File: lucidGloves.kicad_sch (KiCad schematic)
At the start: 25 parts, among them J1 USB_C_Receptacle_PowerOnly_6P, J10 Conn_01x05_Male, J11 Conn_01x05_Male, J12 Conn_01x19_Female, J13 Conn_01x05_Male, J14 Conn_01x03_Male, J15 Conn_01x03_Male, J16 Conn_01x03_Male, J17 Conn_01x03_Male, J18 Conn_01x03_Male, J2 USB_C_Receptacle_PowerOnly_6P, J3 Conn_01x05_Male, J4 Conn_01x05_Male, J5 Conn_01x05_Male, J6 Conn_01x16_Male, J7 Conn_01x08_Male, J8 Conn_01x19_Female, J9 Conn_01x05_Male, SW1 SW_MEC_5E

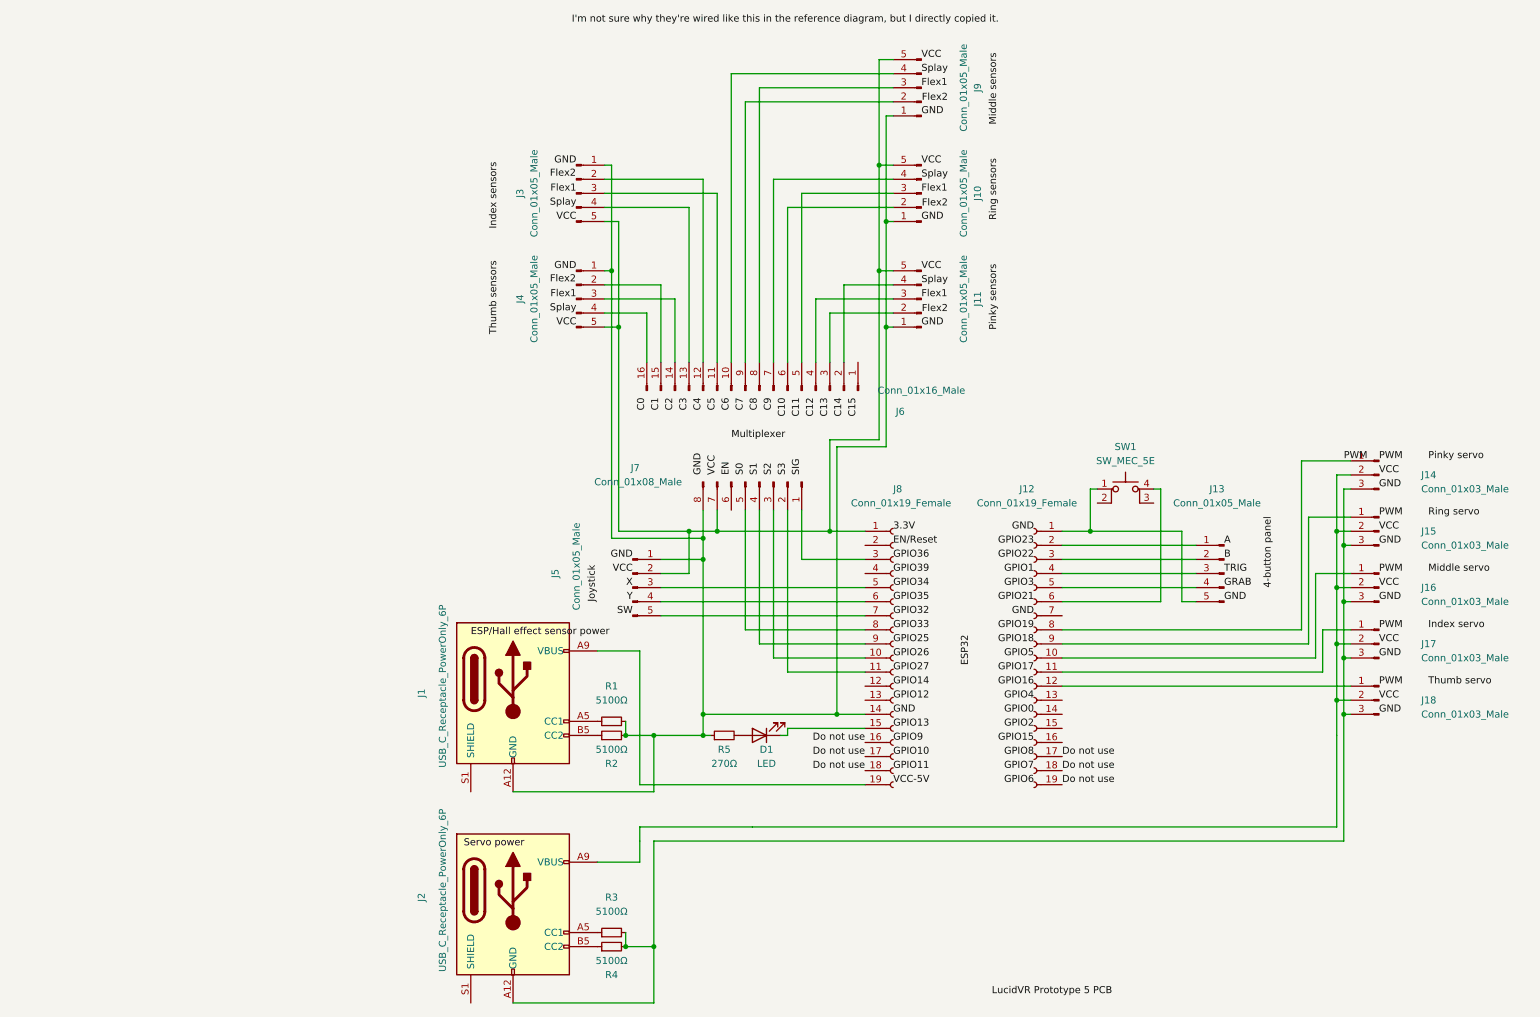
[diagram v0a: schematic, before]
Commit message: Fix all ERC errors and warnings
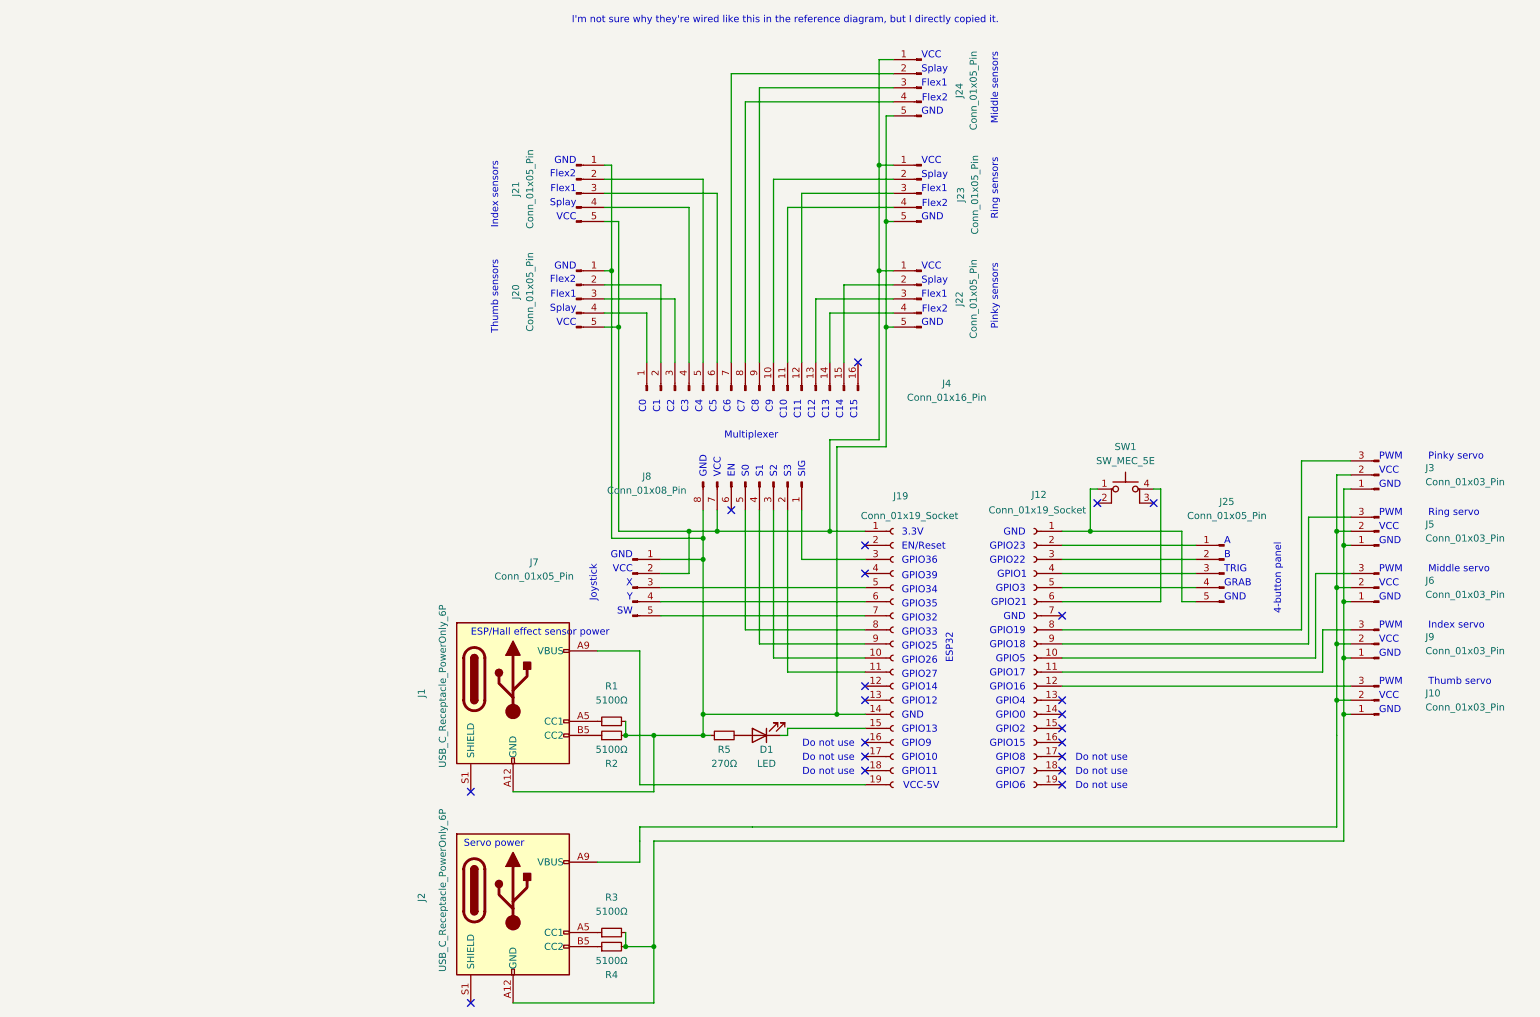
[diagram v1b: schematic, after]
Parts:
- removed J10, J11, J13, J3, J4, J5, J9: Conn_01x05_Male, symbol Connector:Conn_01x05_Male
- removed J12, J8: Conn_01x19_Female, symbol Connector:Conn_01x19_Female
- removed J14, J15, J16, J17, J18: Conn_01x03_Male, symbol Connector:Conn_01x03_Male
- removed J6: Conn_01x16_Male, symbol Connector:Conn_01x16_Male
- removed J7: Conn_01x08_Male, symbol Connector:Conn_01x08_Male
- added J10, J3, J5, J6, J9: Conn_01x03_Pin, symbol Connector:Conn_01x03_Pin
- added J12, J19: Conn_01x19_Socket, symbol Connector:Conn_01x19_Socket
- added J20, J21, J22, J23, J24, J25, J7: Conn_01x05_Pin, symbol Connector:Conn_01x05_Pin
- added J4: Conn_01x16_Pin, symbol Connector:Conn_01x16_Pin
- added J8: Conn_01x08_Pin, symbol Connector:Conn_01x08_Pin
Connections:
- net at J1.A12 (GND), J1.B12 (GND), R1.2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: now also J19.14 (Pin_14), J20.1 (Pin_1), J21.1 (Pin_1), J22.5 (Pin_5), J23.5 (Pin_5), J24.5 (Pin_5), J7.1 (Pin_1), J8.8 (Pin_8)
- net at D1.1 (K): now also J19.15 (Pin_15)
- net at J1.A9 (VBUS), J1.B9 (VBUS): now also J19.19 (Pin_19)
- net at J2.A9 (VBUS), J2.B9 (VBUS): now also J10.2 (Pin_2), J3.2 (Pin_2), J5.2 (Pin_2), J6.2 (Pin_2), J9.2 (Pin_2)
- net at J2.A12 (GND), J2.B12 (GND), R3.2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: now also J10.1 (Pin_1), J3.1 (Pin_1), J5.1 (Pin_1), J6.1 (Pin_1), J9.1 (Pin_1)
- net at SW1.1: now also J12.1 (Pin_1), J25.5 (Pin_5)
- net at SW1.4 (A): now also J12.6 (Pin_6)
- new net: J12.10 (Pin_10), J6.3 (Pin_3)
- new net: J12.11 (Pin_11), J9.3 (Pin_3)
- new net: J10.3 (Pin_3), J12.12 (Pin_12)
- new net: J12.2 (Pin_2), J25.1 (Pin_1)
- new net: J12.3 (Pin_3), J25.2 (Pin_2)
- new net: J12.4 (Pin_4), J25.3 (Pin_3)
- new net: J12.5 (Pin_5), J25.4 (Pin_4)
- new net: J12.8 (Pin_8), J3.3 (Pin_3)
- new net: J12.9 (Pin_9), J5.3 (Pin_3)
- new net: J19.1 (Pin_1), J20.5 (Pin_5), J21.5 (Pin_5), J22.1 (Pin_1), J23.1 (Pin_1), J24.1 (Pin_1), J7.2 (Pin_2), J8.7 (Pin_7)
- new net: J22.2 (Pin_2), J4.15 (Pin_15)
- new net: J22.3 (Pin_3), J4.13 (Pin_13)
- new net: J22.4 (Pin_4), J4.14 (Pin_14)
- new net: J20.2 (Pin_2), J4.2 (Pin_2)
- new net: J20.3 (Pin_3), J4.3 (Pin_3)
- new net: J20.4 (Pin_4), J4.1 (Pin_1)
- new net: J21.2 (Pin_2), J4.5 (Pin_5)
- new net: J21.3 (Pin_3), J4.6 (Pin_6)
- new net: J21.4 (Pin_4), J4.4 (Pin_4)
- new net: J19.5 (Pin_5), J7.3 (Pin_3)
- new net: J19.6 (Pin_6), J7.4 (Pin_4)
- new net: J19.7 (Pin_7), J7.5 (Pin_5)
- new net: J23.2 (Pin_2), J4.10 (Pin_10)
- new net: J23.3 (Pin_3), J4.12 (Pin_12)
- new net: J23.4 (Pin_4), J4.11 (Pin_11)
- new net: J19.3 (Pin_3), J8.1 (Pin_1)
- new net: J19.11 (Pin_11), J8.2 (Pin_2)
- new net: J19.10 (Pin_10), J8.3 (Pin_3)
- new net: J19.9 (Pin_9), J8.4 (Pin_4)
- new net: J19.8 (Pin_8), J8.5 (Pin_5)
- new net: J24.2 (Pin_2), J4.7 (Pin_7)
- new net: J24.4 (Pin_4), J4.8 (Pin_8)
- new net: J24.3 (Pin_3), J4.9 (Pin_9)
- no-connect marks 0 -> 21
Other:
- note added: "3.3V"
- note added: "4-button panel"
- note added: "A"
- note added: "B"
- note added: "C0"
- note added: "C1"
- note added: "C10"
- note added: "C11"
- note added: "C12"
- note added: "C13"
- note added: "C14"
- note added: "C15"
- note added: "C2"
- note added: "C3"
- note added: "C4"
- note added: "C5"
- note added: "C6"
- note added: "C7"
- note added: "C8"
- note added: "C9"
- note added: "Do not use"
- note added: "EN"
- note added: "EN/Reset"
- note added: "ESP/Hall effect sensor power"
- note added: "ESP32"
- note added: "Flex1"
- note added: "Flex2"
- note added: "GND"
- note added: "GPIO0"
- note added: "GPIO1"
- note added: "GPIO10"
- note added: "GPIO11"
- note added: "GPIO12"
- note added: "GPIO13"
- note added: "GPIO14"
- note added: "GPIO15"
- note added: "GPIO16"
- note added: "GPIO17"
- note added: "GPIO18"
- note added: "GPIO19"
- note added: "GPIO2"
- note added: "GPIO21"
- note added: "GPIO22"
- note added: "GPIO23"
- note added: "GPIO25"
- note added: "GPIO26"
- note added: "GPIO27"
- note added: "GPIO3"
- note added: "GPIO32"
- note added: "GPIO33"
- note added: "GPIO34"
- note added: "GPIO35"
- note added: "GPIO36"
- note added: "GPIO39"
- note added: "GPIO4"
- note added: "GPIO5"
- note added: "GPIO6"
- note added: "GPIO7"
- note added: "GPIO8"
- note added: "GPIO9"
- note added: "GRAB"
- note added: "I'm not sure why they're wired like this in the reference diagram, but I directly copied it."
- note added: "Index sensors"
- note added: "Index servo"
- note added: "Joystick"
- note added: "Middle sensors"
- note added: "Middle servo"
- note added: "Multiplexer"
- note added: "PWM"
- note added: "Pinky sensors"
- note added: "Pinky servo"
- note added: "Ring sensors"
- note added: "Ring servo"
- note added: "S0"
- note added: "S1"
- note added: "S2"
- note added: "S3"
- note added: "SIG"
- note added: "SW"
- note added: "Servo power"
- note added: "Splay"
- note added: "TRIG"
- note added: "Thumb sensors"
- note added: "Thumb servo"
- note added: "VCC"
- note added: "VCC-5V"
- note added: "X"
- note added: "Y"
- title: (none) -> LucidVR Prototype 5 PCB

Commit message: Add footprints to schematic
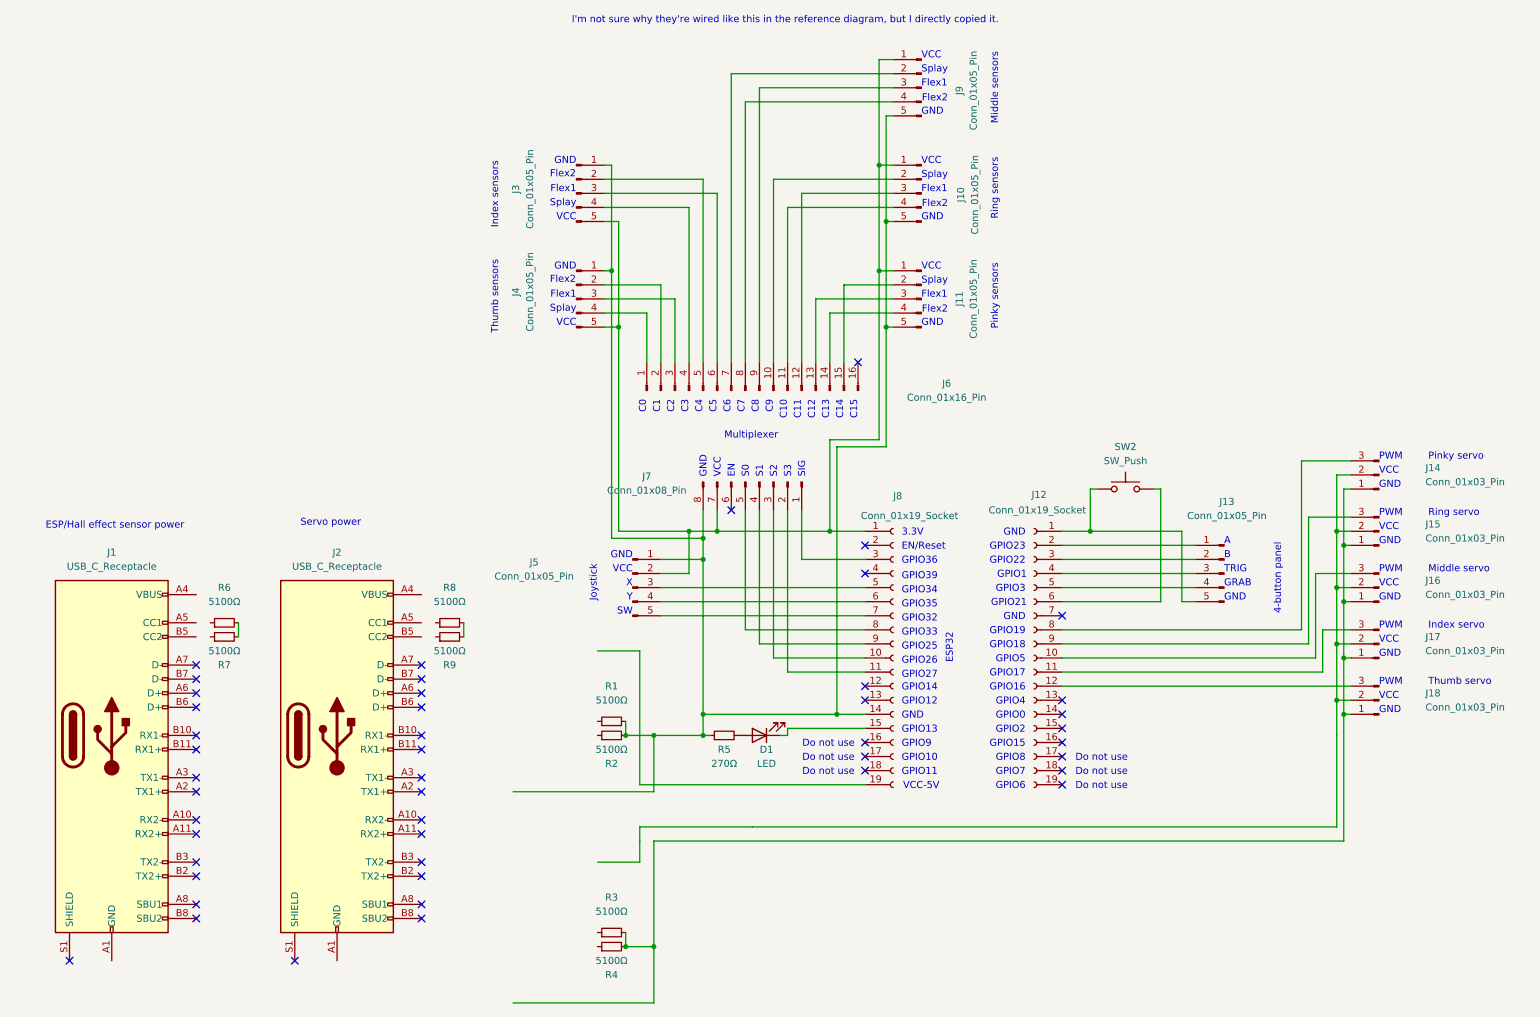
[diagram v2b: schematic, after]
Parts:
- removed J1, J2: USB_C_Receptacle_PowerOnly_6P, symbol Connector:USB_C_Receptacle_PowerOnly_6P
- removed SW1: SW_MEC_5E, symbol Switch:SW_MEC_5E
- added J1, J2: USB_C_Receptacle, symbol Connector:USB_C_Receptacle
- added R6, R7, R8, R9: 5100Ω, Resistor_SMD:R_0603_1608Metric, symbol Device:R_Small
- added SW2: SW_Push, Button_Switch_THT:SW_TH_Tactile_Omron_B3F-10xx, symbol Switch:SW_Push
- D1: footprint (none) -> LED_THT:LED_D5.0mm
- J10: renamed from J23; footprint (none) -> Connector_PinHeader_2.54mm:PinHeader_1x05_P2.54mm_Vertical
- J11: renamed from J22; footprint (none) -> Connector_PinHeader_2.54mm:PinHeader_1x05_P2.54mm_Vertical
- J12: footprint (none) -> Connector_PinSocket_2.54mm:PinSocket_1x19_P2.54mm_Vertical
- J13: renamed from J25; footprint (none) -> Connector_PinHeader_2.54mm:PinHeader_1x05_P2.54mm_Vertical
- J14: renamed from J3; footprint (none) -> Connector_PinHeader_2.54mm:PinHeader_1x03_P2.54mm_Vertical
- J15: renamed from J5; footprint (none) -> Connector_PinHeader_2.54mm:PinHeader_1x03_P2.54mm_Vertical
- J16: renamed from J6; footprint (none) -> Connector_PinHeader_2.54mm:PinHeader_1x03_P2.54mm_Vertical
- J17: renamed from J9; footprint (none) -> Connector_PinHeader_2.54mm:PinHeader_1x03_P2.54mm_Vertical
- J18: renamed from J10; footprint (none) -> Connector_PinHeader_2.54mm:PinHeader_1x03_P2.54mm_Vertical
- J3: renamed from J21; footprint (none) -> Connector_PinHeader_2.54mm:PinHeader_1x05_P2.54mm_Vertical
- J4: renamed from J20; footprint (none) -> Connector_PinHeader_2.54mm:PinHeader_1x05_P2.54mm_Vertical
- J5: renamed from J7; footprint (none) -> Connector_PinHeader_2.54mm:PinHeader_1x05_P2.54mm_Vertical
- J6: renamed from J4; footprint (none) -> Connector_PinHeader_2.00mm:PinHeader_1x16_P2.00mm_Vertical
- J7: renamed from J8; footprint (none) -> Connector_PinHeader_2.00mm:PinHeader_1x08_P2.00mm_Vertical
- J8: renamed from J19; footprint (none) -> Connector_PinSocket_2.54mm:PinSocket_1x19_P2.54mm_Vertical
- J9: renamed from J24; footprint (none) -> Connector_PinHeader_2.54mm:PinHeader_1x05_P2.54mm_Vertical
- R1, R2, R3, R4, R5: footprint (none) -> Resistor_SMD:R_0603_1608Metric
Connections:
- net at J12.1 (Pin_1), J13.5 (Pin_5): now also SW2.1
- net at J12.6 (Pin_6): now also SW2.2
- new net: R8.2, R9.2
- new net: J1.A1 (GND), J1.A12 (GND), J1.B1 (GND), J1.B12 (GND)
- new net: J1.A4 (VBUS), J1.A9 (VBUS), J1.B4 (VBUS), J1.B9 (VBUS)
- new net: J2.A1 (GND), J2.A12 (GND), J2.B1 (GND), J2.B12 (GND)
- new net: J2.A4 (VBUS), J2.A9 (VBUS), J2.B4 (VBUS), J2.B9 (VBUS)
- new net: R6.2, R7.2
- no-connect marks 21 -> 47

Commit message: Mostly lay out PCB
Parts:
- removed R2, R3, R4, R6, R8, R9: 5100Ω, Resistor_SMD:R_0603_1608Metric, symbol Device:R_Small
- added H1, H2, H3, H4, H5, H6: MountingHole, MountingHole:MountingHole_3.2mm_M3, symbol Mechanical:MountingHole
- J1, J2: footprint (none) -> Connector_USB:USB_C_Receptacle_Molex_105450-0101
- J6: footprint Connector_PinHeader_2.00mm:PinHeader_1x16_P2.00mm_Vertical -> Connector_PinHeader_2.54mm:PinHeader_1x16_P2.54mm_Vertical
- J7: footprint Connector_PinHeader_2.00mm:PinHeader_1x08_P2.00mm_Vertical -> Connector_PinHeader_2.54mm:PinHeader_1x08_P2.54mm_Vertical
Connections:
- net at R1.1: now also J2.A5 (CC1), J2.B5 (CC2)
- net at J10.5 (Pin_5), J11.5 (Pin_5), J3.1 (Pin_1)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: now also J2.A1 (GND), J2.A12 (GND), J2.B1 (GND), J2.B12 (GND)
- net at J1.A1 (GND), J1.A12 (GND), J1.B1 (GND)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: now also J14.1 (Pin_1), J15.1 (Pin_1), J16.1 (Pin_1), J17.1 (Pin_1), J18.1 (Pin_1), R7.2
- net at J1.A4 (VBUS), J1.A9 (VBUS), J1.B4 (VBUS)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: now also J14.2 (Pin_2), J15.2 (Pin_2), J16.2 (Pin_2), J17.2 (Pin_2), J18.2 (Pin_2)
- net at J1.A5 (CC1): now also J1.B5 (CC2), R7.1
- net at J1.A6 (D+): now also J1.B6 (D+)
- net at J1.A7 (D-): now also J1.B7 (D-)
- net at J2.A4 (VBUS), J2.A9 (VBUS), J2.B4 (VBUS)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: now also J8.19 (Pin_19)
- net at J2.A6 (D+): now also J2.B6 (D+)
- net at J2.A7 (D-): now also J2.B7 (D-)
- no-connect marks 47 -> 39
